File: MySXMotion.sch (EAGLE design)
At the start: 17 parts, among them IC2 BH1750

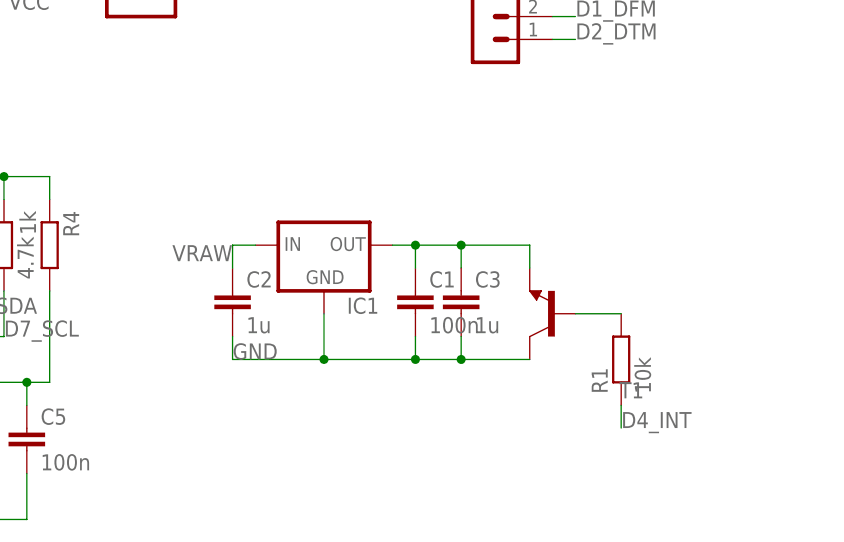
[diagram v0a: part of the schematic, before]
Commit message: add reverse voltage protection
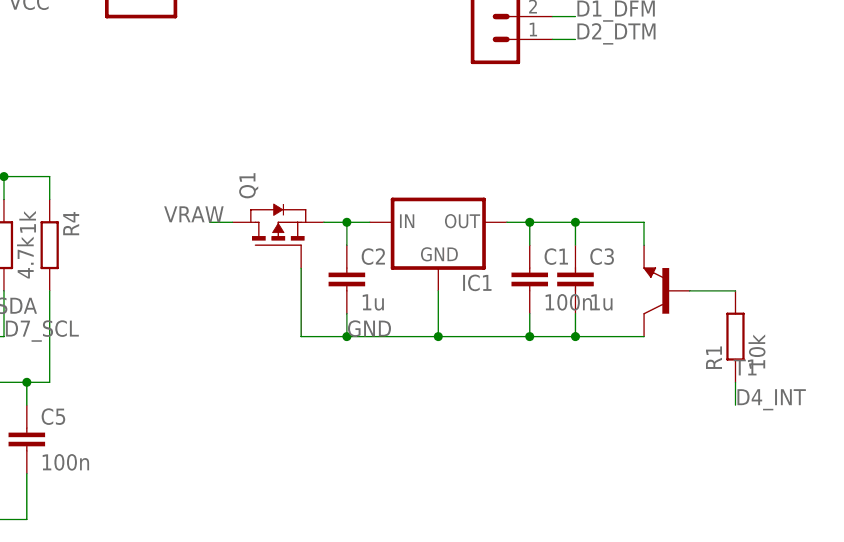
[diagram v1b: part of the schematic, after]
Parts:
- added Q1: (no value), zetex:PMOSSOT23
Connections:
- new net N$4: C2.1, IC1.IN, Q1.S
- net GND: now also Q1.G
- net VRAW: now also Q1.D; no longer C2.1, IC1.IN
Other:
- moved on the sheet: C1, C2, C3, IC1, R1, T1
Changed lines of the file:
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@@
 <part name="J1" library="jumper" deviceset="SJ2W" device=""/>
 <part name="IC2" library="bh1750" deviceset="BH1750" device=""/>
+<part name="Q1" library="zetex" deviceset="PMOSSOT23" device=""/>
 </parts>
 <sheets>
@@
 <instance part="UART" gate="1" x="48.26" y="25.4"/>
 <instance part="X1" gate="G$1" x="10.16" y="58.42"/>
-<instance part="IC1" gate="G$1" x="30.48" y="-2.54"/>
-<instance part="R1" gate="G$1" x="63.5" y="-15.24" rot="R90"/>
-<instance part="C1" gate="G$1" x="40.64" y="-7.62"/>
-<instance part="C2" gate="G$1" x="20.32" y="-7.62"/>
-<instance part="C3" gate="G$1" x="45.72" y="-7.62"/>
-<instance part="T1" gate="G$1" x="55.88" y="-10.16" rot="R180"/>
+<instance part="IC1" gate="G$1" x="43.18" y="0"/>
+<instance part="R1" gate="G$1" x="76.2" y="-12.7" rot="R90"/>
+<instance part="C1" gate="G$1" x="53.34" y="-5.08"/>
+<instance part="C2" gate="G$1" x="33.02" y="-5.08"/>
+<instance part="C3" gate="G$1" x="58.42" y="-5.08"/>
+<instance part="T1" gate="G$1" x="68.58" y="-7.62" rot="R180"/>
 <instance part="R2" gate="G$1" x="-10.16" y="-2.54" rot="R90"/>
 <instance part="R3" gate="G$1" x="-5.08" y="-2.54" rot="R90"/>
@@
 <instance part="J1" gate="G$1" x="-15.24" y="0"/>
 <instance part="IC2" gate="G$1" x="-22.86" y="-17.78"/>
+<instance part="Q1" gate="A" x="25.4" y="0" rot="R90"/>
 </instances>
 <busses>
@@
 <segment>
 <pinref part="R1" gate="G$1" pin="1"/>
-<wire x1="63.5" y1="-20.32" x2="63.5" y2="-22.86" width="0.1524" layer="91"/>
-<label x="63.5" y="-22.86" size="1.778" layer="95"/>
+<wire x1="76.2" y1="-17.78" x2="76.2" y2="-20.32" width="0.1524" layer="91"/>
+<label x="76.2" y="-20.32" size="1.778" layer="95"/>
 </segment>
 </net>
@@
 <segment>
 <pinref part="C2" gate="G$1" pin="2"/>
-<wire x1="20.32" y1="-12.7" x2="20.32" y2="-15.24" width="0.1524" layer="91"/>
+<wire x1="33.02" y1="-10.16" x2="33.02" y2="-12.7" width="0.1524" layer="91"/>
 <pinref part="C1" gate="G$1" pin="2"/>
-<wire x1="20.32" y1="-15.24" x2="30.48" y2="-15.24" width="0.1524" layer="91"/>
-<wire x1="30.48" y1="-15.24" x2="40.64" y2="-15.24" width="0.1524" layer="91"/>
-<wire x1="40.64" y1="-15.24" x2="40.64" y2="-12.7" width="0.1524" layer="91"/>
+<wire x1="33.02" y1="-12.7" x2="43.18" y2="-12.7" width="0.1524" layer="91"/>
+<wire x1="43.18" y1="-12.7" x2="53.34" y2="-12.7" width="0.1524" layer="91"/>
+<wire x1="53.34" y1="-12.7" x2="53.34" y2="-10.16" width="0.1524" layer="91"/>
 <pinref part="C3" gate="G$1" pin="2"/>
-<wire x1="45.72" y1="-12.7" x2="45.72" y2="-15.24" width="0.1524" layer="91"/>
-<wire x1="45.72" y1="-15.24" x2="40.64" y2="-15.24" width="0.1524" layer="91"/>
+<wire x1="58.42" y1="-10.16" x2="58.42" y2="-12.7" width="0.1524" layer="91"/>
+<wire x1="58.42" y1="-12.7" x2="53.34" y2="-12.7" width="0.1524" layer="91"/>
 <pinref part="IC1" gate="G$1" pin="GND"/>
-<wire x1="30.48" y1="-10.16" x2="30.48" y2="-15.24" width="0.1524" layer="91"/>
-<label x="20.32" y="-15.24" size="1.778" layer="95"/>
+<wire x1="43.18" y1="-7.62" x2="43.18" y2="-12.7" width="0.1524" layer="91"/>
+<label x="33.02" y="-12.7" size="1.778" layer="95"/>
 <pinref part="T1" gate="G$1" pin="C"/>
-<wire x1="53.34" y1="-15.24" x2="45.72" y2="-15.24" width="0.1524" layer="91"/>
-<junction x="30.48" y="-15.24"/>
-<junction x="40.64" y="-15.24"/>
-<junction x="45.72" y="-15.24"/>
+<wire x1="66.04" y1="-12.7" x2="58.42" y2="-12.7" width="0.1524" layer="91"/>
+<junction x="43.18" y="-12.7"/>
+<junction x="53.34" y="-12.7"/>
+<junction x="58.42" y="-12.7"/>
+<pinref part="Q1" gate="A" pin="G"/>
+<wire x1="33.02" y1="-12.7" x2="27.94" y2="-12.7" width="0.1524" layer="91"/>
+<wire x1="27.94" y1="-12.7" x2="27.94" y2="-5.08" width="0.1524" layer="91"/>
+<junction x="33.02" y="-12.7"/>
 </segment>
 </net>
@@
 </segment>
 <segment>
-<pinref part="IC1" gate="G$1" pin="IN"/>
-<pinref part="C2" gate="G$1" pin="1"/>
-<wire x1="22.86" y1="-2.54" x2="20.32" y2="-2.54" width="0.1524" layer="91"/>
-<wire x1="20.32" y1="-2.54" x2="20.32" y2="-5.08" width="0.1524" layer="91"/>
-<label x="20.32" y="-2.54" size="1.778" layer="95" rot="R180"/>
+<pinref part="Q1" gate="A" pin="D"/>
+<wire x1="20.32" y1="0" x2="17.78" y2="0" width="0.1524" layer="91"/>
+<label x="12.7" y="0" size="1.778" layer="95"/>
 </segment>
 </net>
@@
 <pinref part="IC1" gate="G$1" pin="OUT"/>
 <pinref part="C1" gate="G$1" pin="1"/>
-<wire x1="38.1" y1="-2.54" x2="40.64" y2="-2.54" width="0.1524" layer="91"/>
-<wire x1="40.64" y1="-2.54" x2="40.64" y2="-5.08" width="0.1524" layer="91"/>
+<wire x1="50.8" y1="0" x2="53.34" y2="0" width="0.1524" layer="91"/>
+<wire x1="53.34" y1="0" x2="53.34" y2="-2.54" width="0.1524" layer="91"/>
 <pinref part="C3" gate="G$1" pin="1"/>
-<wire x1="40.64" y1="-2.54" x2="45.72" y2="-2.54" width="0.1524" layer="91"/>
-<wire x1="45.72" y1="-2.54" x2="45.72" y2="-5.08" width="0.1524" layer="91"/>
-<wire x1="45.72" y1="-2.54" x2="53.34" y2="-2.54" width="0.1524" layer="91"/>
+<wire x1="53.34" y1="0" x2="58.42" y2="0" width="0.1524" layer="91"/>
+<wire x1="58.42" y1="0" x2="58.42" y2="-2.54" width="0.1524" layer="91"/>
+<wire x1="58.42" y1="0" x2="66.04" y2="0" width="0.1524" layer="91"/>
 <pinref part="T1" gate="G$1" pin="E"/>
-<wire x1="53.34" y1="-5.08" x2="53.34" y2="-2.54" width="0.1524" layer="91"/>
-<junction x="40.64" y="-2.54"/>
-<junction x="45.72" y="-2.54"/>
+<wire x1="66.04" y1="-2.54" x2="66.04" y2="0" width="0.1524" layer="91"/>
+<junction x="53.34" y="0"/>
+<junction x="58.42" y="0"/>
 </segment>
 </net>
@@
 <pinref part="R1" gate="G$1" pin="2"/>
 <pinref part="T1" gate="G$1" pin="B"/>
-<wire x1="63.5" y1="-10.16" x2="58.42" y2="-10.16" width="0.1524" layer="91"/>
-</segment>
-</net>
+<wire x1="76.2" y1="-7.62" x2="71.12" y2="-7.62" width="0.1524" layer="91"/>
+</segment>
+</net>
+<net name="N$4" class="1">
+<segment>
+<pinref part="Q1" gate="A" pin="S"/>
+<pinref part="IC1" gate="G$1" pin="IN"/>
+<wire x1="30.48" y1="0" x2="33.02" y2="0" width="0.1524" layer="91"/>
+<pinref part="C2" gate="G$1" pin="1"/>
+<wire x1="33.02" y1="0" x2="35.56" y2="0" width="0.1524" layer="91"/>
+<wire x1="33.02" y1="-2.54" x2="33.02" y2="0" width="0.1524" layer="91"/>
+<junction x="33.02" y="0"/>
+</segment>
+</net>

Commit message: add documentation
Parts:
- renumbered BMP280 to I2C, T1 to IC3
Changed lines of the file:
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@@
 </classes>
 <parts>
-<part name="BMP280" library="con-lstb" deviceset="MA04-1" device=""/>
+<part name="I2C" library="con-lstb" deviceset="MA04-1" device=""/>
 <part name="ISP" library="con-lstb" deviceset="MA03-2" device=""/>
 <part name="UART" library="con-lstb" deviceset="MA04-1" device=""/>
@@
 <part name="C2" library="rcl" deviceset="C-EU" device="C0603" value="1u"/>
 <part name="C3" library="rcl" deviceset="C-EU" device="C0805" value="1u"/>
-<part name="T1" library="transistor" deviceset="*-NPN-" device="TO5"/>
+<part name="IC3" library="transistor" deviceset="*-NPN-" device="TO5"/>
 <part name="R2" library="rcl" deviceset="R-EU_" device="R0603" value="4.7k"/>
 <part name="R3" library="rcl" deviceset="R-EU_" device="R0603" value="4.7k"/>
@@
 </plain>
 <instances>
-<instance part="BMP280" gate="1" x="48.26" y="43.18"/>
+<instance part="I2C" gate="1" x="48.26" y="43.18"/>
 <instance part="ISP" gate="1" x="10.16" y="27.94"/>
 <instance part="UART" gate="1" x="48.26" y="25.4"/>
@@
 <instance part="C2" gate="G$1" x="33.02" y="-5.08"/>
 <instance part="C3" gate="G$1" x="58.42" y="-5.08"/>
-<instance part="T1" gate="G$1" x="68.58" y="-7.62" rot="R180"/>
-<instance part="R2" gate="G$1" x="-10.16" y="-2.54" rot="R90"/>
-<instance part="R3" gate="G$1" x="-5.08" y="-2.54" rot="R90"/>
+<instance part="IC3" gate="G$1" x="68.58" y="-7.62" smashed="yes" rot="R180">
+<attribute name="NAME" x="71.12" y="-2.54" size="1.778" layer="95" rot="R180"/>
+<attribute name="VALUE" x="78.74" y="-12.7" size="1.778" layer="96" rot="R180"/>
+</instance>
+<instance part="R2" gate="G$1" x="-10.16" y="-2.54" smashed="yes" rot="R90">
+<attribute name="NAME" x="-6.5786" y="-6.35" size="1.778" layer="95" rot="R90"/>
+<attribute name="VALUE" x="-6.858" y="-1.27" size="1.778" layer="96" rot="R90"/>
+</instance>
+<instance part="R3" gate="G$1" x="-5.08" y="-2.54" smashed="yes" rot="R90">
+<attribute name="NAME" x="-1.4986" y="-6.35" size="1.778" layer="95" rot="R90"/>
+<attribute name="VALUE" x="-1.778" y="-1.27" size="1.778" layer="96" rot="R90"/>
+</instance>
 <instance part="C4" gate="G$1" x="-27.94" y="-2.54" rot="R180"/>
-<instance part="R4" gate="G$1" x="0" y="-2.54" rot="R270"/>
+<instance part="R4" gate="G$1" x="0" y="-2.54" smashed="yes" rot="R270">
+<attribute name="NAME" x="1.4986" y="-3.81" size="1.778" layer="95" rot="R270"/>
+<attribute name="VALUE" x="1.778" y="1.27" size="1.778" layer="96" rot="R270"/>
+</instance>
 <instance part="C5" gate="G$1" x="-2.54" y="-22.86"/>
 <instance part="J1" gate="G$1" x="-15.24" y="0"/>
@@
 <net name="VCC" class="1">
 <segment>
-<pinref part="BMP280" gate="1" pin="4"/>
+<pinref part="I2C" gate="1" pin="4"/>
 <wire x1="55.88" y1="45.72" x2="58.42" y2="45.72" width="0.1524" layer="91"/>
 <label x="58.42" y="45.72" size="1.778" layer="95"/>
@@
 <net name="D7_SCL" class="0">
 <segment>
-<pinref part="BMP280" gate="1" pin="2"/>
+<pinref part="I2C" gate="1" pin="2"/>
 <wire x1="55.88" y1="40.64" x2="58.42" y2="40.64" width="0.1524" layer="91"/>
 <label x="58.42" y="40.64" size="1.778" layer="95"/>
@@
 <wire x1="-12.7" y1="-12.7" x2="-5.08" y2="-12.7" width="0.1524" layer="91"/>
 <wire x1="-5.08" y1="-12.7" x2="-5.08" y2="-7.62" width="0.1524" layer="91"/>
-<label x="-5.08" y="-12.7" size="1.778" layer="95"/>
+<label x="-15.24" y="-15.24" size="1.778" layer="95"/>
 </segment>
 </net>
@@
 <net name="D8_SDA" class="0">
 <segment>
-<pinref part="BMP280" gate="1" pin="1"/>
+<pinref part="I2C" gate="1" pin="1"/>
 <wire x1="55.88" y1="38.1" x2="58.42" y2="38.1" width="0.1524" layer="91"/>
 <label x="58.42" y="38.1" size="1.778" layer="95"/>
@@
 <wire x1="-12.7" y1="-10.16" x2="-10.16" y2="-10.16" width="0.1524" layer="91"/>
 <wire x1="-10.16" y1="-10.16" x2="-10.16" y2="-7.62" width="0.1524" layer="91"/>
-<label x="-10.16" y="-10.16" size="1.778" layer="95"/>
+<label x="-15.24" y="-12.7" size="1.778" layer="95"/>
 </segment>
 </net>
@@
 <net name="GND" class="1">
 <segment>
-<pinref part="BMP280" gate="1" pin="3"/>
+<pinref part="I2C" gate="1" pin="3"/>
 <wire x1="55.88" y1="43.18" x2="58.42" y2="43.18" width="0.1524" layer="91"/>
 <label x="58.42" y="43.18" size="1.778" layer="95"/>
@@
 <wire x1="43.18" y1="-7.62" x2="43.18" y2="-12.7" width="0.1524" layer="91"/>
 <label x="33.02" y="-12.7" size="1.778" layer="95"/>
-<pinref part="T1" gate="G$1" pin="C"/>
+<pinref part="IC3" gate="G$1" pin="C"/>
 <wire x1="66.04" y1="-12.7" x2="58.42" y2="-12.7" width="0.1524" layer="91"/>
 <junction x="43.18" y="-12.7"/>
@@
 <wire x1="58.42" y1="0" x2="58.42" y2="-2.54" width="0.1524" layer="91"/>
 <wire x1="58.42" y1="0" x2="66.04" y2="0" width="0.1524" layer="91"/>
-<pinref part="T1" gate="G$1" pin="E"/>
+<pinref part="IC3" gate="G$1" pin="E"/>
 <wire x1="66.04" y1="-2.54" x2="66.04" y2="0" width="0.1524" layer="91"/>
 <junction x="53.34" y="0"/>
@@
 <segment>
 <pinref part="R1" gate="G$1" pin="2"/>
-<pinref part="T1" gate="G$1" pin="B"/>
+<pinref part="IC3" gate="G$1" pin="B"/>
 <wire x1="76.2" y1="-7.62" x2="71.12" y2="-7.62" width="0.1524" layer="91"/>
 </segment>
